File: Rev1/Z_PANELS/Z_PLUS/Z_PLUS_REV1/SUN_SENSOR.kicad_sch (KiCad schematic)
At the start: 32 parts, among them IC1 LTC4316IDD#PBF, Q1 BSS138, Q2 BSS138, Q4 BSS138, Q5 BSS138, U1 OPT4001DTST

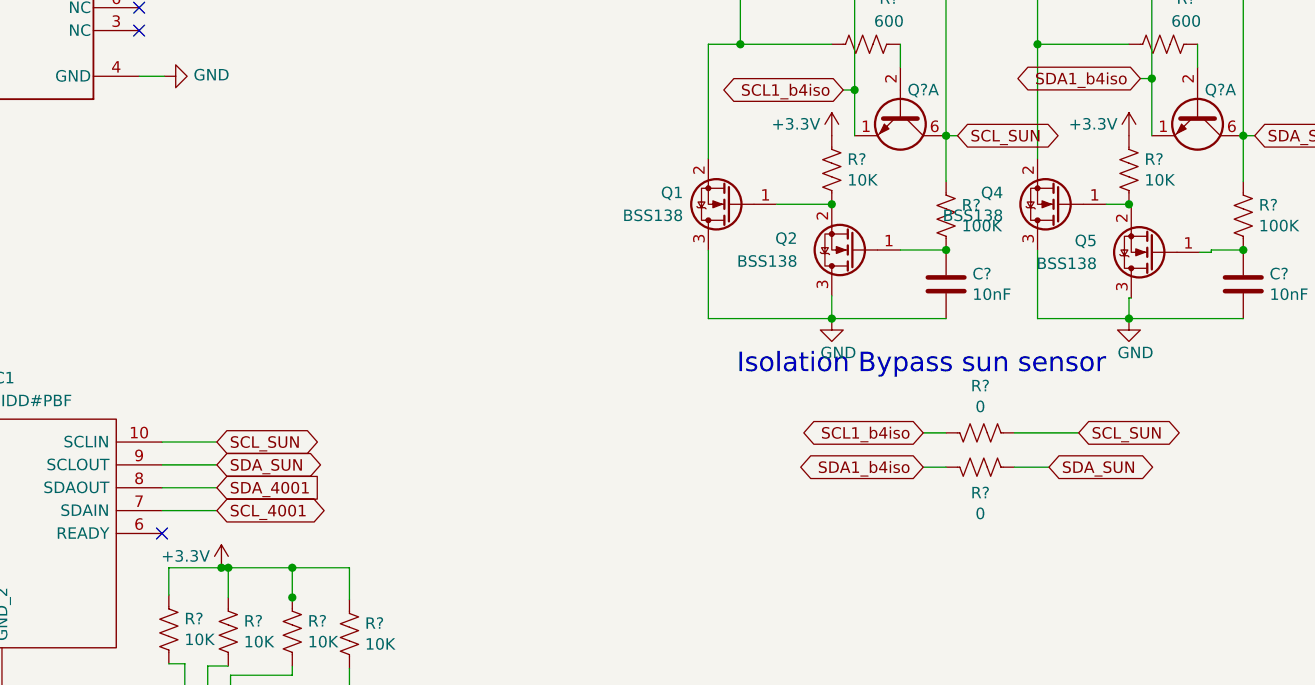
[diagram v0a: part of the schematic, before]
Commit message: fixed bug in Z minus
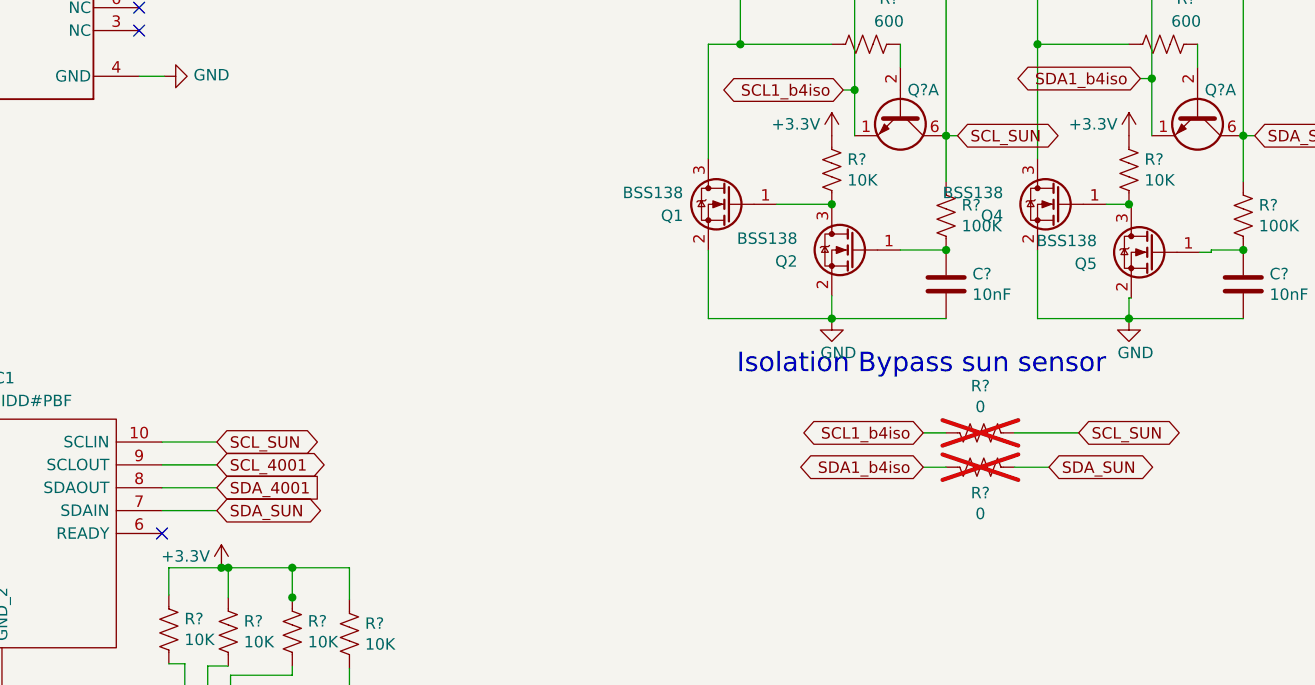
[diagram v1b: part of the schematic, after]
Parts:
- R? (x2): now not fitted; now left out of the parts list
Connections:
- net GND: now also Q1.2 (S), Q2.2 (S), Q4.2 (S), Q5.2 (S); no longer Q1.3 (D), Q2.3 (D), Q4.3 (D), Q5.3 (D)
- net SCL_4001: now also IC1.9 (SCLOUT); no longer IC1.7 (SDAIN)
- net SDA_SUN: now also IC1.7 (SDAIN); no longer IC1.9 (SCLOUT)
- net at Q4.1 (G), R?.1: now also Q5.3 (D); no longer Q5.2 (S)
- net at Q?.5 (B2), R?.2, R?.2: now also Q4.3 (D); no longer Q4.2 (S)
- net at Q1.1 (G), R?.1: now also Q2.3 (D); no longer Q2.2 (S)
- net at Q?.5 (B2), R?.1, R?.2: now also Q1.3 (D); no longer Q1.2 (S)
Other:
- moved on the sheet: Q1, Q2, Q4, Q5
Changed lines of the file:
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@@
+    (stroke (width 0) (type default))
+  )
+  (wire (pts (xy 108.712 122.682) (xy 114.808 122.682))
     (stroke (width 0) (type default))
   )
@@
     (stroke (width 0) (type default))
   )
-  (wire (pts (xy 114.808 120.142) (xy 108.712 120.142))
-    (stroke (width 0) (type default))
-  )
   (wire (pts (xy 218.694 64.516) (xy 218.694 77.216))
     (stroke (width 0) (type default))
@@
     (stroke (width 0) (type default))
   )
+  (wire (pts (xy 108.712 120.142) (xy 114.808 120.142))
+    (stroke (width 0) (type default))
+  )
   (wire (pts (xy 184.404 78.486) (xy 185.674 78.486))
     (stroke (width 0) (type default))
@@
     (stroke (width 0) (type default))
   )
+  (wire (pts (xy 108.712 117.602) (xy 114.808 117.602))
+    (stroke (width 0) (type default))
+  )
   (wire (pts (xy 63.246 71.882) (xy 65.532 71.882))
     (stroke (width 0) (type default))
@@
     (stroke (width 0) (type default))
   )
-  (wire (pts (xy 114.808 117.602) (xy 108.712 117.602))
-    (stroke (width 0) (type default))
-  )
   (wire (pts (xy 73.152 127.762) (xy 70.104 127.762))
     (stroke (width 0) (type default))
@@
     (stroke (width 0) (type default))
   )
-  (wire (pts (xy 114.808 122.682) (xy 108.712 122.682))
-    (stroke (width 0) (type default))
-  )
   (wire (pts (xy 228.854 56.896) (xy 228.854 49.276))
     (stroke (width 0) (type default))
@@
     (stroke (width 0) (type default))
   )
+  (wire (pts (xy 108.712 125.222) (xy 114.808 125.222))
+    (stroke (width 0) (type default))
+  )
   (wire (pts (xy 73.152 107.188) (xy 73.152 117.602))
     (stroke (width 0) (type default))
@@
   )
   (wire (pts (xy 216.154 91.186) (xy 213.614 91.186))
-    (stroke (width 0) (type default))
-  )
-  (wire (pts (xy 114.808 125.222) (xy 108.712 125.222))
     (stroke (width 0) (type default))
   )
@@
     )
   )
-  (global_label "SDA_SUN" (shape bidirectional) (at 114.808 120.142 0)
+  (global_label "SDA_SUN" (shape bidirectional) (at 114.808 125.222 0)
     (effects (font (size 1.27 1.27)) (justify left))
-    (property "Intersheetrefs" "${INTERSHEET_REFS}" (at 114.808 120.142 0)
+    (property "Intersheetrefs" "${INTERSHEET_REFS}" (at 114.808 125.222 0)
       (effects (font (size 1.27 1.27)) hide)
     )
@@
     )
   )
-  (global_label "SCL_4001" (shape bidirectional) (at 114.808 125.222 0)
+  (global_label "SCL_4001" (shape bidirectional) (at 114.808 120.142 0)
     (effects (font (size 1.27 1.27)) (justify left))
-    (property "Intersheetrefs" "${INTERSHEET_REFS}" (at 114.808 125.222 0)
+    (property "Intersheetrefs" "${INTERSHEET_REFS}" (at 114.808 120.142 0)
       (effects (font (size 1.27 1.27)) hide)
     )
@@
     )
   )
-  (symbol (lib_id "Transistor_FET:BSS138") (at 185.674 96.266 180) (unit 1)
-    (in_bom yes) (on_board yes) (dnp no) (fields_autoplaced)
-    (property "Reference" "Q2" (at 179.324 94.996 0)
+  (symbol (lib_id "Transistor_FET:BSS138") (at 185.674 96.266 0) (mirror y) (unit 1)
+    (in_bom yes) (on_board yes) (dnp no)
+    (property "Reference" "Q2" (at 179.324 97.536 0)
       (effects (font (size 1.27 1.27)) (justify left))
     )
-    (property "Value" "BSS138" (at 179.324 97.536 0)
+    (property "Value" "BSS138" (at 179.324 94.996 0)
       (effects (font (size 1.27 1.27)) (justify left))
     )
-    (property "Footprint" "Package_TO_SOT_SMD:SOT-23" (at 180.594 94.361 0)
+    (property "Footprint" "Package_TO_SOT_SMD:SOT-23" (at 180.594 98.171 0)
       (effects (font (size 1.27 1.27) italic) (justify left) hide)
     )
@@
   )
   (symbol (lib_id "Device:R_US") (at 199.644 120.396 90) (mirror x) (unit 1)
-    (in_bom yes) (on_board yes) (dnp no)
+    (in_bom no) (on_board yes) (dnp yes)
     (property "Reference" "R?" (at 199.644 123.2662 90)
       (effects (font (size 1.27 1.27)))
@@
     )
   )
-  (symbol (lib_id "Transistor_FET:BSS138") (at 218.948 96.52 180) (unit 1)
-    (in_bom yes) (on_board yes) (dnp no) (fields_autoplaced)
-    (property "Reference" "Q5" (at 212.598 95.25 0)
+  (symbol (lib_id "Transistor_FET:BSS138") (at 218.948 96.52 0) (mirror y) (unit 1)
+    (in_bom yes) (on_board yes) (dnp no)
+    (property "Reference" "Q5" (at 212.598 97.79 0)
       (effects (font (size 1.27 1.27)) (justify left))
     )
-    (property "Value" "BSS138" (at 212.598 97.79 0)
+    (property "Value" "BSS138" (at 212.598 95.25 0)
       (effects (font (size 1.27 1.27)) (justify left))
     )
-    (property "Footprint" "Package_TO_SOT_SMD:SOT-23" (at 213.868 94.615 0)
+    (property "Footprint" "Package_TO_SOT_SMD:SOT-23" (at 213.868 98.425 0)
       (effects (font (size 1.27 1.27) italic) (justify left) hide)
     )
@@
     )
   )
-  (symbol (lib_id "Transistor_FET:BSS138") (at 208.534 91.186 180) (unit 1)
-    (in_bom yes) (on_board yes) (dnp no) (fields_autoplaced)
-    (property "Reference" "Q4" (at 202.184 89.916 0)
+  (symbol (lib_id "Transistor_FET:BSS138") (at 208.534 91.186 0) (mirror y) (unit 1)
+    (in_bom yes) (on_board yes) (dnp no)
+    (property "Reference" "Q4" (at 202.184 92.456 0)
       (effects (font (size 1.27 1.27)) (justify left))
     )
-    (property "Value" "BSS138" (at 202.184 92.456 0)
+    (property "Value" "BSS138" (at 202.184 89.916 0)
       (effects (font (size 1.27 1.27)) (justify left))
     )
-    (property "Footprint" "Package_TO_SOT_SMD:SOT-23" (at 203.454 89.281 0)
+    (property "Footprint" "Package_TO_SOT_SMD:SOT-23" (at 203.454 93.091 0)
       (effects (font (size 1.27 1.27) italic) (justify left) hide)
     )
@@
   )
   (symbol (lib_id "Device:R_US") (at 199.644 116.586 90) (mirror x) (unit 1)
-    (in_bom yes) (on_board yes) (dnp no)
+    (in_bom no) (on_board yes) (dnp yes)
     (property "Reference" "R?" (at 199.644 111.379 90)
       (effects (font (size 1.27 1.27)))
@@
     )
   )
-  (symbol (lib_id "Transistor_FET:BSS138") (at 171.958 91.186 180) (unit 1)
-    (in_bom yes) (on_board yes) (dnp no) (fields_autoplaced)
-    (property "Reference" "Q1" (at 166.624 89.916 0)
+  (symbol (lib_id "Transistor_FET:BSS138") (at 171.958 91.186 0) (mirror y) (unit 1)
+    (in_bom yes) (on_board yes) (dnp no)
+    (property "Reference" "Q1" (at 166.624 92.456 0)
       (effects (font (size 1.27 1.27)) (justify left))
     )
-    (property "Value" "BSS138" (at 166.624 92.456 0)
+    (property "Value" "BSS138" (at 166.624 89.916 0)
       (effects (font (size 1.27 1.27)) (justify left))
     )
-    (property "Footprint" "Package_TO_SOT_SMD:SOT-23" (at 166.878 89.281 0)
+    (property "Footprint" "Package_TO_SOT_SMD:SOT-23" (at 166.878 93.091 0)
       (effects (font (size 1.27 1.27) italic) (justify left) hide)
     )

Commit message: fixed bugs and finished Z plus
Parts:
- R? (x8): footprint Resistor_SMD:R_0603_1608Metric -> Resistor_SMD:R_0805_2012Metric
- R? (x8): footprint Resistor_SMD:R_0402_1005Metric -> Resistor_SMD:R_0805_2012Metric
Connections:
- net +3.3v is gone; now on net +3.3V: JP2.3 (B), U1.1 (VDD)
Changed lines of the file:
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@@
       (effects (font (size 1.27 1.27)) (justify right))
     )
-    (property "Footprint" "Resistor_SMD:R_0603_1608Metric" (at 215.138 87.122 90)
+    (property "Footprint" "Resistor_SMD:R_0805_2012Metric" (at 215.138 87.122 90)
       (effects (font (size 1.27 1.27)) hide)
     )
@@
       (effects (font (size 1.27 1.27)) (justify right))
     )
-    (property "Footprint" "Resistor_SMD:R_0402_1005Metric" (at 128.524 138.684 90)
+    (property "Footprint" "Resistor_SMD:R_0805_2012Metric" (at 128.524 138.684 90)
       (effects (font (size 1.27 1.27)) hide)
     )
@@
       (effects (font (size 1.27 1.27)) (justify right))
     )
-    (property "Footprint" "Resistor_SMD:R_0603_1608Metric" (at 224.79 53.34 90)
+    (property "Footprint" "Resistor_SMD:R_0805_2012Metric" (at 224.79 53.34 90)
       (effects (font (size 1.27 1.27)) hide)
     )
@@
       (effects (font (size 1.27 1.27)) (justify right))
     )
-    (property "Footprint" "Resistor_SMD:R_0402_1005Metric" (at 115.062 138.43 90)
+    (property "Footprint" "Resistor_SMD:R_0805_2012Metric" (at 115.062 138.43 90)
       (effects (font (size 1.27 1.27)) hide)
     )
@@
       (effects (font (size 1.27 1.27)) (justify right))
     )
-    (property "Footprint" "Resistor_SMD:R_0402_1005Metric" (at 227.838 60.452 90)
+    (property "Footprint" "Resistor_SMD:R_0805_2012Metric" (at 227.838 60.452 90)
       (effects (font (size 1.27 1.27)) hide)
     )
@@
       (effects (font (size 1.27 1.27)) (justify right))
     )
-    (property "Footprint" "Resistor_SMD:R_0402_1005Metric" (at 64.77 110.744 90)
+    (property "Footprint" "Resistor_SMD:R_0805_2012Metric" (at 64.77 110.744 90)
       (effects (font (size 1.27 1.27)) hide)
     )
@@
       (effects (font (size 1.27 1.27)))
     )
-    (property "Footprint" "Resistor_SMD:R_0603_1608Metric" (at 187.198 72.39 90)
+    (property "Footprint" "Resistor_SMD:R_0805_2012Metric" (at 187.198 72.39 90)
       (effects (font (size 1.27 1.27)) hide)
     )
@@
         (path "/97119169-578f-44be-8822-faf8f0e4fcd6/06756695-4e8e-4b7d-905d-85546769f1f1"
           (reference "R16") (unit 1)
+        )
+      )
+    )
+  )
+  (symbol (lib_id "power:+3.3V") (at 54.61 64.008 0) (mirror y) (unit 1)
+    (in_bom yes) (on_board yes) (dnp no)
+    (property "Reference" "#PWR?" (at 54.61 67.818 0)
+      (effects (font (size 1.27 1.27)) hide)
+    )
+    (property "Value" "+3.3V" (at 53.34 62.738 0)
+      (effects (font (size 1.27 1.27)) (justify left))
+    )
+    (property "Footprint" "" (at 54.61 64.008 0)
+      (effects (font (size 1.27 1.27)) hide)
+    )
+    (property "Datasheet" "" (at 54.61 64.008 0)
+      (effects (font (size 1.27 1.27)) hide)
+    )
+    (pin "1")
+    (instances
+      (project "xpanel"
+        (path "/30bf83b4-3f3b-46f2-ac0f-8077e2dc1b24"
+          (reference "#PWR?") (unit 1)
+        )
+      )
+      (project "Z_PLUS_REV1"
+        (path "/39cf28b0-d395-4333-bc0e-a98538893595/02f51ab8-9bf5-460b-98ef-c53969a9f1c8"
+          (reference "#PWR034") (unit 1)
+        )
+      )
+      (project "Xpanel_V1_final"
+        (path "/97119169-578f-44be-8822-faf8f0e4fcd6"
+          (reference "#PWR011") (unit 1)
+        )
+        (path "/97119169-578f-44be-8822-faf8f0e4fcd6/db306d3f-1ab7-4e38-afab-c78bdb56c587"
+          (reference "#PWR031") (unit 1)
+        )
+        (path "/97119169-578f-44be-8822-faf8f0e4fcd6/06756695-4e8e-4b7d-905d-85546769f1f1"
+          (reference "#PWR031") (unit 1)
         )
       )
@@
       (effects (font (size 1.27 1.27)) (justify right))
     )
-    (property "Footprint" "Resistor_SMD:R_0402_1005Metric" (at 64.77 121.158 90)
+    (property "Footprint" "Resistor_SMD:R_0805_2012Metric" (at 64.77 121.158 90)
       (effects (font (size 1.27 1.27)) hide)
     )
@@
       (effects (font (size 1.27 1.27)) (justify right))
     )
-    (property "Footprint" "Resistor_SMD:R_0603_1608Metric" (at 182.118 87.122 90)
+    (property "Footprint" "Resistor_SMD:R_0805_2012Metric" (at 182.118 87.122 90)
       (effects (font (size 1.27 1.27)) hide)
     )
@@
       (effects (font (size 1.27 1.27)) (justify right))
     )
-    (property "Footprint" "Resistor_SMD:R_0402_1005Metric" (at 108.458 138.176 90)
+    (property "Footprint" "Resistor_SMD:R_0805_2012Metric" (at 108.458 138.176 90)
       (effects (font (size 1.27 1.27)) hide)
     )
@@
       (effects (font (size 1.27 1.27)))
     )
-    (property "Footprint" "Resistor_SMD:R_0603_1608Metric" (at 219.71 74.422 90)
+    (property "Footprint" "Resistor_SMD:R_0805_2012Metric" (at 219.71 74.422 90)
       (effects (font (size 1.27 1.27)) hide)
     )
@@
       (effects (font (size 1.27 1.27)) (justify right))
     )
-    (property "Footprint" "Resistor_SMD:R_0603_1608Metric" (at 227.838 92.202 90)
+    (property "Footprint" "Resistor_SMD:R_0805_2012Metric" (at 227.838 92.202 90)
       (effects (font (size 1.27 1.27)) hide)
     )
@@
       (effects (font (size 1.27 1.27)) (justify right))
     )
-    (property "Footprint" "Resistor_SMD:R_0402_1005Metric" (at 122.174 138.43 90)
+    (property "Footprint" "Resistor_SMD:R_0805_2012Metric" (at 122.174 138.43 90)
       (effects (font (size 1.27 1.27)) hide)
     )
@@
       (effects (font (size 1.27 1.27)) (justify right))
     )
-    (property "Footprint" "Resistor_SMD:R_0603_1608Metric" (at 191.77 53.34 90)
+    (property "Footprint" "Resistor_SMD:R_0805_2012Metric" (at 191.77 53.34 90)
       (effects (font (size 1.27 1.27)) hide)
     )
@@
     )
   )
+  (symbol (lib_id "power:+3.3V") (at 52.578 81.534 0) (mirror y) (unit 1)
+    (in_bom yes) (on_board yes) (dnp no)
+    (property "Reference" "#PWR?" (at 52.578 85.344 0)
+      (effects (font (size 1.27 1.27)) hide)
+    )
+    (property "Value" "+3.3V" (at 51.308 80.264 0)
+      (effects (font (size 1.27 1.27)) (justify left))
+    )
+    (property "Footprint" "" (at 52.578 81.534 0)
+      (effects (font (size 1.27 1.27)) hide)
+    )
+    (property "Datasheet" "" (at 52.578 81.534 0)
+      (effects (font (size 1.27 1.27)) hide)
+    )
+    (pin "1")
+    (instances
+      (project "xpanel"
+        (path "/30bf83b4-3f3b-46f2-ac0f-8077e2dc1b24"
+          (reference "#PWR?") (unit 1)
+        )
+      )
+      (project "Z_PLUS_REV1"
+        (path "/39cf28b0-d395-4333-bc0e-a98538893595/02f51ab8-9bf5-460b-98ef-c53969a9f1c8"
+          (reference "#PWR035") (unit 1)
+        )
+      )
+      (project "Xpanel_V1_final"
+        (path "/97119169-578f-44be-8822-faf8f0e4fcd6"
+          (reference "#PWR011") (unit 1)
+        )
+        (path "/97119169-578f-44be-8822-faf8f0e4fcd6/db306d3f-1ab7-4e38-afab-c78bdb56c587"
+          (reference "#PWR031") (unit 1)
+        )
+        (path "/97119169-578f-44be-8822-faf8f0e4fcd6/06756695-4e8e-4b7d-905d-85546769f1f1"
+          (reference "#PWR031") (unit 1)
+        )
+      )
+    )
+  )
   (symbol (lib_id "Device:R_US") (at 195.834 60.706 180) (unit 1)
     (in_bom yes) (on_board yes) (dnp no)
@@
       (effects (font (size 1.27 1.27)) (justify right))
     )
-    (property "Footprint" "Resistor_SMD:R_0402_1005Metric" (at 194.818 60.452 90)
+    (property "Footprint" "Resistor_SMD:R_0805_2012Metric" (at 194.818 60.452 90)
       (effects (font (size 1.27 1.27)) hide)
     )
@@
       (effects (font (size 1.27 1.27)) (justify right))
     )
-    (property "Footprint" "Resistor_SMD:R_0603_1608Metric" (at 194.818 92.202 90)
-      (effects (font (size 1.27 1.27)) hide)
-    )
+    (property "Footprint" "Resistor_SMD:R_0805_2012Metric" (at 194.818 92.202 90)
+      (effects (font (size 1.27 1.27)) hide)
+    )

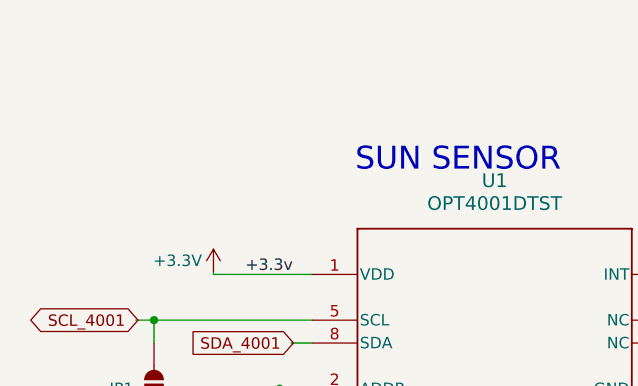
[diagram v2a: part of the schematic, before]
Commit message: made diode changes and schematic changes
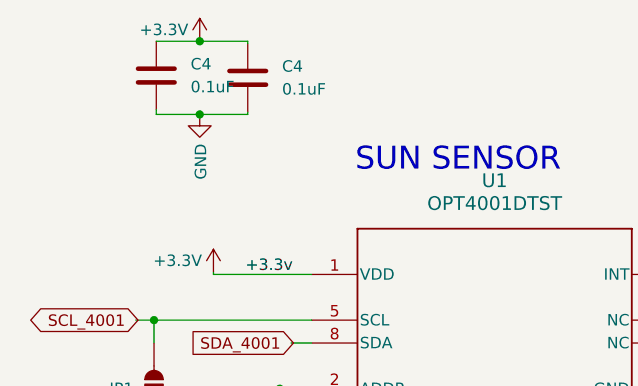
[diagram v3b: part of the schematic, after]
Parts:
- added C4 (x2): 0.1uF, Capacitor_SMD:C_0805_2012Metric, symbol PCM_Capacitor_AKL:C_0805
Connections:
- net +3.3V: now also C4.1, C4.1
- net GND: now also C4.2, C4.2
